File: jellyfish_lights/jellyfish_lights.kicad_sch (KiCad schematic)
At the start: 24 parts, among them Q1 AO3400A, SW1 tilt switch, U1 SN74LVC1G14DBV

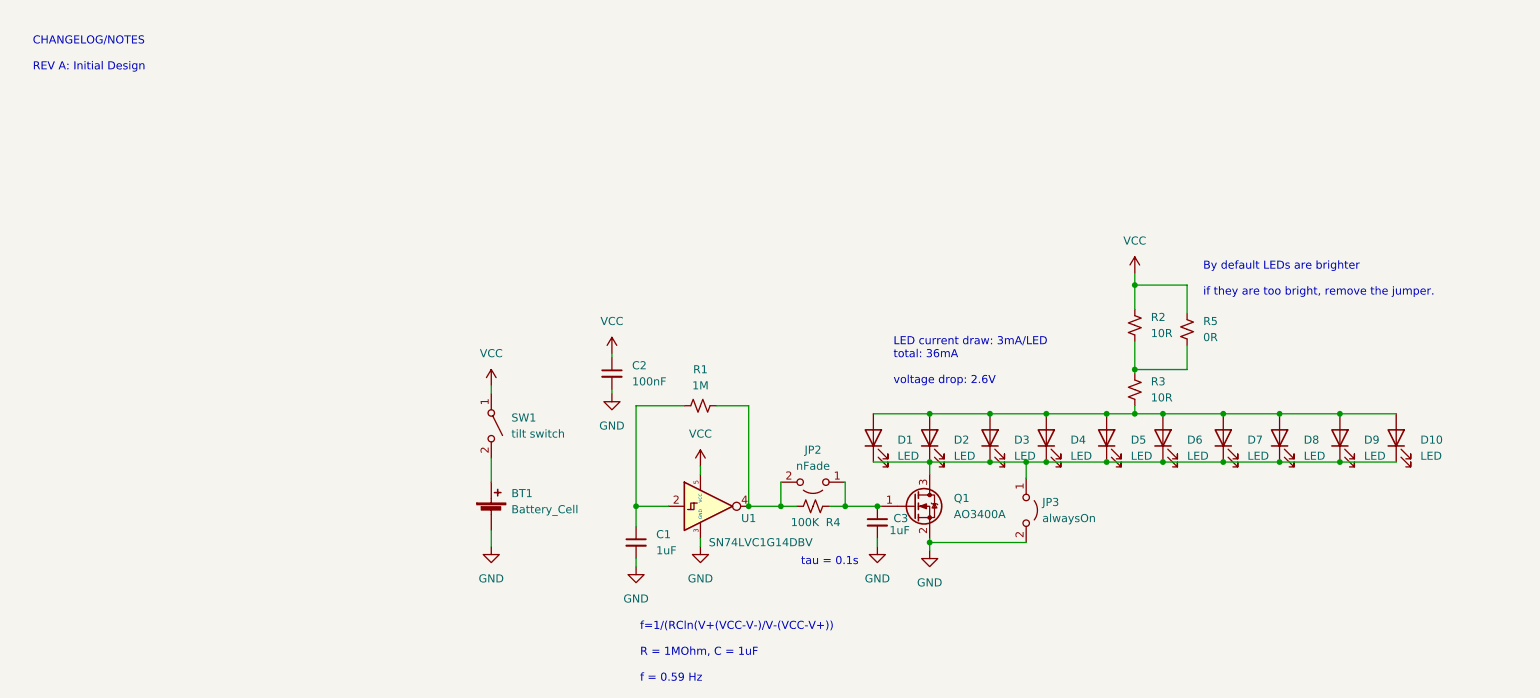
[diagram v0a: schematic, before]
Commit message: edited BOM
 Changed C3 to 4.7uF from 1uF
		Changed R4 to 330K from 100K
          Changed LEDs to C84265
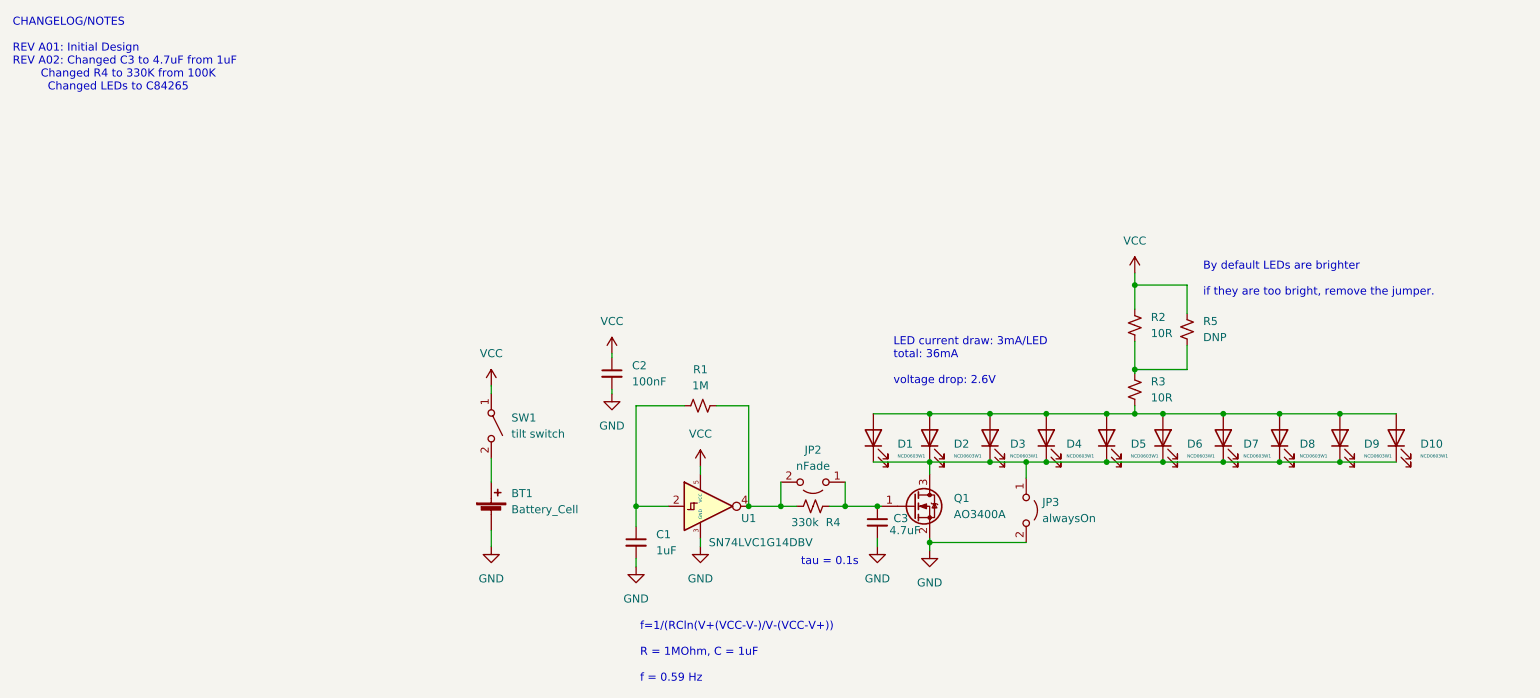
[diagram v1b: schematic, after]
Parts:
- C3: value 1uF -> 4.7uF; LCSC C52923 -> C23733
- D1, D10, D2, D3, D4, D5, D6, D7, D8, D9: value LED -> NCD0603W1; LCSC C2290 -> C84265
- R4: value 100K -> 330k; LCSC C25741 -> C25778
- R5: value 0R -> DNP; LCSC C17168 -> (none)
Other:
- note added: "CHANGELOG/NOTES REV A01: Initial Design REV A02: Changed C3 to 4.7uF from 1uF Changed R4 to 330K from 100K Changed LEDs to C84265"
- note removed: "CHANGELOG/NOTES REV A: Initial Design"

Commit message: Rev B01
Changed board shape
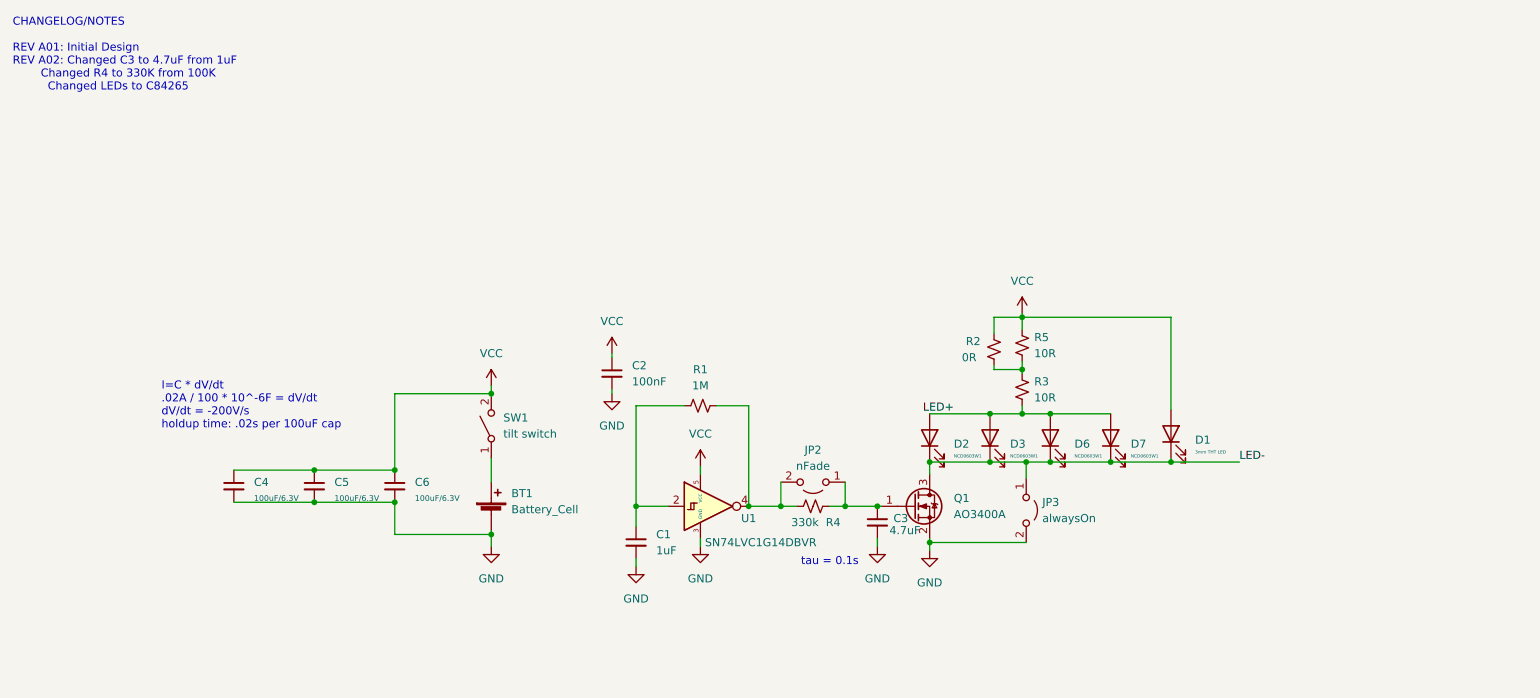
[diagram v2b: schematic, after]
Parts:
- removed D10, D4, D5, D8, D9: NCD0603W1, LED_SMD:LED_0603_1608Metric, symbol Device:LED
- added C4, C5, C6: 100uF/6.3V, Capacitor_SMD:C_1206_3216Metric, symbol Device:C_Small
- D1: value NCD0603W1 -> 3mm THT LED; footprint LED_SMD:LED_0603_1608Metric -> LED_THT:LED_D5.0mm_FlatTop
- R2: value 10R -> 0R; LCSC C25077 -> C21189
- R3: LCSC C25077 -> C22859
- R5: value DNP -> 10R; LCSC (none) -> C22859
- U1: value SN74LVC1G14DBV -> SN74LVC1G14DBVR
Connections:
- net GND: now also C4.2, C5.2, C6.2
- net VCC: now also D1.2 (A), R2.2, SW1.2 (B), C4.1, C5.1, C6.1; no longer R2.1, SW1.1 (A)
- net LED-: now reaches D1.1 (K), D2.1 (K), D3.1 (K), D6.1 (K), D7.1 (K), JP3.1 (A), Q1.3 (D)
- net LED+: now reaches D2.2 (A), D3.2 (A), D6.2 (A), D7.2 (A), R3.2
- net LED+: no longer D1.2 (A)
- net at R3.1, R5.2: now also R2.1; no longer R2.2
- net at BT1.1 (+): now also SW1.1 (A); no longer SW1.2 (B)
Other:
- note added: "I=C * dV/dt .02A / 100 * 10^-6F = dV/dt dV/dt = -200V/s holdup time: .02s per 100uF cap"
- note removed: "By default LEDs are brighter if they are too bright, remove the jumper."
- note removed: "LED current draw: 3mA/LED total: 36mA voltage drop: 2.6V"
- note removed: "f=1/(RCln(V+(VCC-V-)/V-(VCC-V+)) R = 1MOhm, C = 1uF f = 0.59 Hz"
- moved on the sheet: D6, D7, R3, SW1

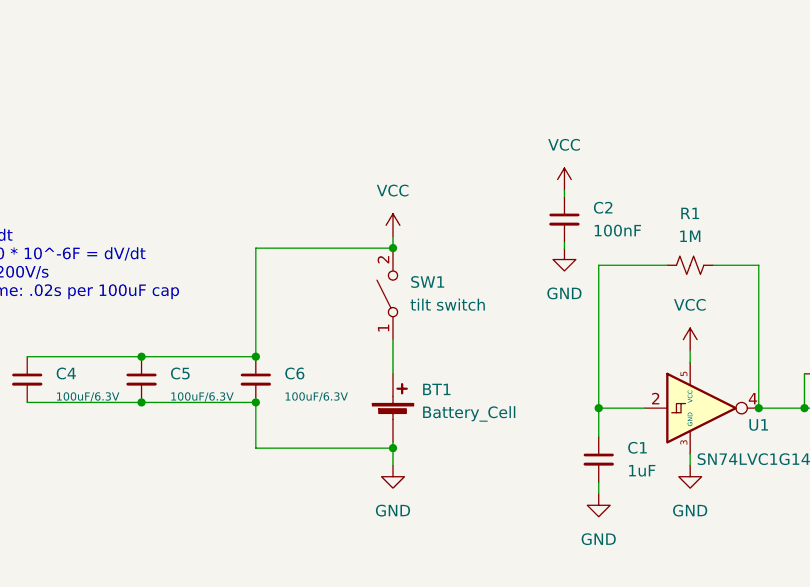
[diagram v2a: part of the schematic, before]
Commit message: Rev C01
-Edited THT footprints to accommodate easier soldering (moved away from BT1)
-Added SW2 to prevent turn-on events while not spinning
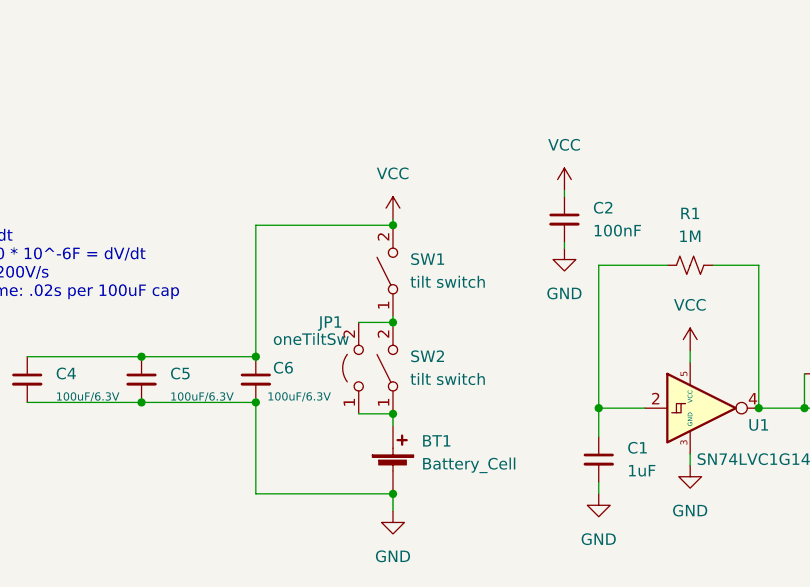
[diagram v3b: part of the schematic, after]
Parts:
- added JP1: oneTiltSw, Jumper:SolderJumper-2_P1.3mm_Open_TrianglePad1.0x1.5mm, symbol Jumper:Jumper_2_Open
- added SW2: tilt switch, WS_LCSC_Mechanical:tilt_switch, symbol Switch:SW_SPST
- SW1: footprint Capacitor_THT:C_Radial_D6.3mm_H5.0mm_P2.50mm -> WS_LCSC_Mechanical:tilt_switch
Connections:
- net at BT1.1 (+): now also JP1.1 (A), SW2.1 (A); no longer SW1.1 (A)
- new net: JP1.2 (B), SW1.1 (A), SW2.2 (B)
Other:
- moved on the sheet: BT1, SW1

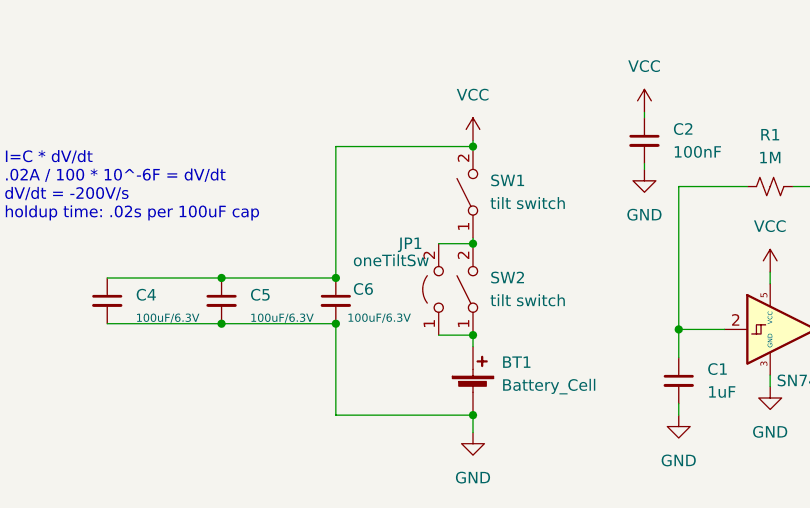
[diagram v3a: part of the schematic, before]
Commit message: changed jumper to 0R resistor for ignoreSW2
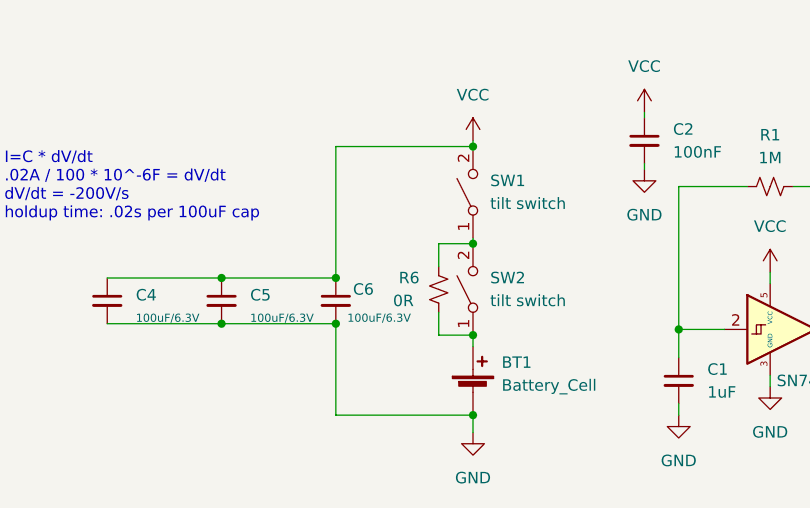
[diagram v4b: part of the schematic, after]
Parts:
- removed JP1: oneTiltSw, Jumper:SolderJumper-2_P1.3mm_Open_TrianglePad1.0x1.5mm, symbol Jumper:Jumper_2_Open
- added R6: 0R, Resistor_SMD:R_0603_1608Metric, symbol Device:R_Small_US
- C2: LCSC C1525 -> (none)
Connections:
- net at BT1.1 (+), SW2.1 (A): now also R6.1
- net at SW1.1 (A), SW2.2 (B): now also R6.2
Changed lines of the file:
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@@
 (kicad_sch (version 20211123) (generator eeschema)
-  (paper "A4")
+  (paper "A")
   (title_block
     (title "Main")
@@
     (stroke (width 0) (type default) (color 0 0 0 0))
   )
+  (wire (pts (xy 88.265 89.535) (xy 88.265 92.075))
+    (stroke (width 0) (type default) (color 0 0 0 0))
+  )
   (wire (pts (xy 76.835 71.12) (xy 76.835 85.725))
     (stroke (width 0) (type default) (color 0 0 0 0))
@@
   )
   (wire (pts (xy 171.45 64.135) (xy 171.45 61.595))
+    (stroke (width 0) (type default) (color 0 0 0 0))
+  )
+  (wire (pts (xy 88.265 81.915) (xy 88.265 84.455))
     (stroke (width 0) (type default) (color 0 0 0 0))
   )
@@
     (pin "3")
   )
+  (symbol (lib_id "Device:R_Small_US") (at 88.265 86.995 180) (unit 1)
+    (in_bom yes) (on_board yes)
+    (property "Reference" "R6" (id 0) (at 83.82 85.725 0)
+      (effects (font (size 1.27 1.27)) (justify right))
+    )
+    (property "Value" "0R" (id 1) (at 83.185 88.265 0)
+      (effects (font (size 1.27 1.27)) (justify right))
+    )
+    (property "Footprint" "Resistor_SMD:R_0603_1608Metric" (id 2) (at 88.265 86.995 0)
+      (effects (font (size 1.27 1.27)) hide)
+    )
+    (property "Datasheet" "~" (id 3) (at 88.265 86.995 0)
+      (effects (font (size 1.27 1.27)) hide)
+    )
+    (property "LCSC" "C21189" (id 4) (at 88.265 86.995 0)
+      (effects (font (size 1.27 1.27)) hide)
+    )
+    (pin "1")
+    (pin "2")
+  )
   (symbol (lib_id "power:VCC") (at 125.095 85.09 0) (unit 1)
     (in_bom yes) (on_board yes) (fields_autoplaced)
@@
       (effects (font (size 1.27 1.27)) hide)
     )
-    (property "Datasheet" "~" (id 3) (at 170.815 80.645 0)
+    (property "Datasheet" "https://datasheet.lcsc.com/lcsc/2008201032_Foshan-NationStar-Optoelectronics-NCD0603W1_C84265.pdf" (id 3) (at 170.815 80.645 0)
       (effects (font (size 1.27 1.27)) hide)
     )
@@
     (pin "2")
   )
-  (symbol (lib_id "Jumper:Jumper_2_Open") (at 88.265 86.995 90) (unit 1)
-    (in_bom yes) (on_board yes)
-    (property "Reference" "JP1" (id 0) (at 83.82 81.915 90)
-      (effects (font (size 1.27 1.27)) (justify right))
-    )
-    (property "Value" "oneTiltSw" (id 1) (at 78.74 83.82 90)
-      (effects (font (size 1.27 1.27)) (justify right))
-    )
-    (property "Footprint" "Jumper:SolderJumper-2_P1.3mm_Open_TrianglePad1.0x1.5mm" (id 2) (at 88.265 86.995 0)
-      (effects (font (size 1.27 1.27)) hide)
-    )
-    (property "Datasheet" "~" (id 3) (at 88.265 86.995 0)
-      (effects (font (size 1.27 1.27)) hide)
-    )
-    (pin "1")
-    (pin "2")
-  )
   (symbol (lib_id "power:GND") (at 111.125 73.66 0) (unit 1)
     (in_bom yes) (on_board yes) (fields_autoplaced)
@@
       (effects (font (size 1.27 1.27)) hide)
     )
-    (property "Datasheet" "https://datasheet.lcsc.com/lcsc/2012181809_MYOUNG-MY-2032-05_C964829.pdf" (id 3) (at 92.075 96.901 90)
+    (property "Datasheet" "https://www.digikey.com/en/products/detail/adam-tech/BH-67D-5/13537750" (id 3) (at 92.075 96.901 90)
       (effects (font (size 1.27 1.27)) hide)
     )
@@
       (effects (font (size 1.27 1.27)) hide)
     )
-    (property "Datasheet" "~" (id 3) (at 199.39 80.01 0)
+    (property "Datasheet" "https://www.amazon.com/Transparent-Lighting-Electronics-Components-Emitting/dp/B01BV2OTLG/ref=rvi_sccl_3/134-4055070-4854936?pd_rd_w=at3BW&content-id=amzn1.sym.f5690a4d-f2bb-45d9-9d1b-736fee412437&pf_rd_p=f5690a4d-f2bb-45d9-9d1b-736fee412437&pf_rd_r=R9D1N0Z28W6CH4MTZT4Z&pd_rd_wg=FNkjX&pd_rd_r=aa135567-7d66-457f-91bd-df994876f1cd&pd_rd_i=B01BV2OTLG&psc=1" (id 3) (at 199.39 80.01 0)
       (effects (font (size 1.27 1.27)) hide)
     )
@@
       (effects (font (size 1.27 1.27)) hide)
     )
-    (property "Datasheet" "~" (id 3) (at 189.865 80.645 0)
+    (property "Datasheet" "https://datasheet.lcsc.com/lcsc/2008201032_Foshan-NationStar-Optoelectronics-NCD0603W1_C84265.pdf" (id 3) (at 189.865 80.645 0)
       (effects (font (size 1.27 1.27)) hide)
     )
@@
       (effects (font (size 1.27 1.27)) hide)
     )
-    (property "Datasheet" "https://datasheet.lcsc.com/lcsc/2110191530_XKB-Connectivity-SW-520DS-AB12G_C2905288.pdf" (id 3) (at 92.075 76.2 0)
+    (property "Datasheet" "https://www.amazon.com/HiLetgo-Vibration-Shaking-Position-Switches/dp/B00M1PMYCE/" (id 3) (at 92.075 76.2 0)
       (effects (font (size 1.27 1.27)) hide)
     )
@@
       (effects (font (size 1.27 1.27)) hide)
     )
-    (property "LCSC" "C1525" (id 4) (at 111.125 70.485 0)
+    (property "LCSC" "" (id 4) (at 111.125 70.485 0)
       (effects (font (size 1.27 1.27)) hide)
     )
@@
       (effects (font (size 1.27 1.27)) hide)
     )
-    (property "Datasheet" "https://datasheet.lcsc.com/lcsc/2110191530_XKB-Connectivity-SW-520DS-AB12G_C2905288.pdf" (id 3) (at 92.075 86.995 0)
+    (property "Datasheet" "https://www.amazon.com/HiLetgo-Vibration-Shaking-Position-Switches/dp/B00M1PMYCE/" (id 3) (at 92.075 86.995 0)
       (effects (font (size 1.27 1.27)) hide)
     )
@@
       (effects (font (size 1.27 1.27)) hide)
     )
-    (property "Datasheet" "~" (id 3) (at 180.34 80.645 0)
+    (property "Datasheet" "https://datasheet.lcsc.com/lcsc/2008201032_Foshan-NationStar-Optoelectronics-NCD0603W1_C84265.pdf" (id 3) (at 180.34 80.645 0)
       (effects (font (size 1.27 1.27)) hide)
     )
@@
       (effects (font (size 1.27 1.27)) hide)
     )
-    (property "Datasheet" "~" (id 3) (at 161.29 80.645 0)
+    (property "Datasheet" "https://datasheet.lcsc.com/lcsc/2008201032_Foshan-NationStar-Optoelectronics-NCD0603W1_C84265.pdf" (id 3) (at 161.29 80.645 0)
       (effects (font (size 1.27 1.27)) hide)
     )
@@
       (reference "D7") (unit 1) (value "NCD0603W1") (footprint "LED_SMD:LED_0603_1608Metric")
     )
-    (path "/4e96d57c-c828-4d40-a73a-73020df795a8"
-      (reference "JP1") (unit 1) (value "oneTiltSw") (footprint "Jumper:SolderJumper-2_P1.3mm_Open_TrianglePad1.0x1.5mm")
-    )
     (path "/1dcee5a4-4839-48cd-9205-d2533438cf0e"
       (reference "JP2") (unit 1) (value "nFade") (footprint "Jumper:SolderJumper-2_P1.3mm_Open_TrianglePad1.0x1.5mm")
@@
       (reference "R5") (unit 1) (value "10R") (footprint "Resistor_SMD:R_0603_1608Metric")
     )
+    (path "/115c8e86-c44c-49a7-bc69-7044c5ce83c9"
+      (reference "R6") (unit 1) (value "0R") (footprint "Resistor_SMD:R_0603_1608Metric")
+    )
     (path "/9cb160c0-5456-4bd7-aa7f-b9388d25eb35"

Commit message: Updated BOM/POS file
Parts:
- C2: LCSC (none) -> C1525
- C3: LCSC C23733 -> C1525
- C4, C5, C6: LCSC C15008 -> (none)
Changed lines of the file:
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@@
       (effects (font (size 1.27 1.27)) hide)
     )
-    (property "LCSC" "C23733" (id 4) (at 153.035 93.98 0)
+    (property "LCSC" "C1525" (id 4) (at 153.035 93.98 0)
       (effects (font (size 1.27 1.27)) hide)
     )
@@
       (effects (font (size 1.27 1.27)) hide)
     )
-    (property "LCSC" "" (id 4) (at 111.125 70.485 0)
+    (property "LCSC" "C1525" (id 4) (at 111.125 70.485 0)
       (effects (font (size 1.27 1.27)) hide)
     )
@@
       (effects (font (size 1.27 1.27)) hide)
     )
-    (property "LCSC" "C15008" (id 4) (at 51.435 88.265 0)
+    (property "LCSC" "" (id 4) (at 51.435 88.265 0)
       (effects (font (size 1.27 1.27)) hide)
     )
@@
       (effects (font (size 1.27 1.27)) hide)
     )
-    (property "LCSC" "C15008" (id 4) (at 76.835 88.265 0)
+    (property "LCSC" "" (id 4) (at 76.835 88.265 0)
       (effects (font (size 1.27 1.27)) hide)
     )
@@
       (effects (font (size 1.27 1.27)) hide)
     )
-    (property "LCSC" "C15008" (id 4) (at 64.135 88.265 0)
-      (effects (font (size 1.27 1.27)) hide)
-    )
+    (property "LCSC" "" (id 4) (at 64.135 88.265 0)
+      (effects (font (size 1.27 1.27)) hide)
+    )

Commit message: fixing LCSC numbers
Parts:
- C3: LCSC C1525 -> C23733
- C4, C5, C6: value 100uF/6.3V -> DNP
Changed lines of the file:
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@@
       (effects (font (size 1.27 1.27)) hide)
     )
-    (property "LCSC" "C1525" (id 4) (at 153.035 93.98 0)
+    (property "LCSC" "C23733" (id 4) (at 153.035 93.98 0)
       (effects (font (size 1.27 1.27)) hide)
     )
@@
       (effects (font (size 1.27 1.27)) (justify left))
     )
-    (property "Value" "100uF/6.3V" (id 1) (at 54.61 90.1763 0)
+    (property "Value" "DNP" (id 1) (at 54.61 90.1763 0)
       (effects (font (size 0.9 0.9)) (justify left))
     )
@@
       (effects (font (size 1.27 1.27)) (justify left))
     )
-    (property "Value" "100uF/6.3V" (id 1) (at 78.105 90.17 0)
+    (property "Value" "DNP" (id 1) (at 78.105 90.17 0)
       (effects (font (size 0.9 0.9)) (justify left))
     )
@@
       (effects (font (size 1.27 1.27)) (justify left))
     )
-    (property "Value" "100uF/6.3V" (id 1) (at 67.31 90.1763 0)
+    (property "Value" "DNP" (id 1) (at 67.31 90.1763 0)
       (effects (font (size 0.9 0.9)) (justify left))
     )
@@
     )
     (path "/cfe137de-fae2-4a91-b461-54f69d1fbbcc"
-      (reference "C4") (unit 1) (value "100uF/6.3V") (footprint "Capacitor_SMD:C_1206_3216Metric")
+      (reference "C4") (unit 1) (value "DNP") (footprint "Capacitor_SMD:C_1206_3216Metric")
     )
     (path "/e5bbd94a-b1f6-4abc-9ac6-e94744718bc3"
-      (reference "C5") (unit 1) (value "100uF/6.3V") (footprint "Capacitor_SMD:C_1206_3216Metric")
+      (reference "C5") (unit 1) (value "DNP") (footprint "Capacitor_SMD:C_1206_3216Metric")
     )
     (path "/daadd0ef-6aaf-45e5-931b-ff448dc0e123"
-      (reference "C6") (unit 1) (value "100uF/6.3V") (footprint "Capacitor_SMD:C_1206_3216Metric")
+      (reference "C6") (unit 1) (value "DNP") (footprint "Capacitor_SMD:C_1206_3216Metric")
     )
     (path "/8efa5a42-1536-4661-bba1-46165b30bac2"
